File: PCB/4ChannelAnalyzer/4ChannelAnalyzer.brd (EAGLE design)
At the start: 91.5 x 91.4 mm, 19 parts, among them U1 ADS1015IDGST, U2 ADS1015IDGST, U3 LM1117MP-3.3, X3 MINI-USB-32005-301

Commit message: adc's ready signal pins / USB connector
connected adc's ready signal pins to uC and wired USB connector
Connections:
- removed net VDD: U1.8, U2.8
- new net EXT_INT_0: LPC1.42, U1.2
- new net EXT_INT_1: LPC1.43, U2.2
- new net N$15: U1.10
- new net N$16: U1.9
- new net N$17: U2.10
- new net N$18: U2.9
- new net N$19: LPC1.36, X3.2
- new net N$20: LPC1.37, X3.3
- new net USB-5V: X3.1
- new net VCC: U1.1, U1.8, U2.8
- net GND: now also U2.1, X3.5
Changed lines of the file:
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@@
 </elements>
 <signals>
-<signal name="VDD">
-<contactref element="U2" pad="8"/>
-<contactref element="U1" pad="8"/>
-<wire x1="67.31" y1="79.0194" x2="67.31" y2="21.2344" width="0" layer="19" extent="1-1"/>
-</signal>
 <signal name="GND">
 <contactref element="LED4" pad="C"/>
@@
 <contactref element="X1" pad="A4"/>
 <contactref element="X1" pad="A2"/>
-<wire x1="80.05" y1="13.435" x2="67.31" y2="16.8656" width="0" layer="19" extent="1-1"/>
-<wire x1="80.05" y1="18.435" x2="80.05" y2="13.435" width="0" layer="19" extent="1-1"/>
-<wire x1="80.05" y1="23.435" x2="80.05" y2="18.435" width="0" layer="19" extent="1-1"/>
-<wire x1="80.05" y1="28.435" x2="80.05" y2="23.435" width="0" layer="19" extent="1-1"/>
-<wire x1="148.59" y1="20.525" x2="80.05" y2="13.435" width="0" layer="19" extent="1-1"/>
-<wire x1="148.59" y1="28.78" x2="148.59" y2="20.525" width="0" layer="19" extent="1-1"/>
-<wire x1="145.415" y1="39.575" x2="148.59" y2="28.78" width="0" layer="19" extent="1-1"/>
-<wire x1="139.065" y1="49.1" x2="145.415" y2="39.575" width="0" layer="19" extent="1-1"/>
+<contactref element="U2" pad="1"/>
+<contactref element="X3" pad="5"/>
 <wire x1="127.635" y1="49.1" x2="139.065" y2="49.1" width="0" layer="19" extent="1-1"/>
+<wire x1="145.415" y1="39.575" x2="139.065" y2="49.1" width="0" layer="19" extent="1-1"/>
+<wire x1="148.59" y1="28.78" x2="145.415" y2="39.575" width="0" layer="19" extent="1-1"/>
+<wire x1="148.59" y1="20.525" x2="148.59" y2="28.78" width="0" layer="19" extent="1-1"/>
 <wire x1="111.76" y1="54.18" x2="127.635" y2="49.1" width="0" layer="19" extent="1-1"/>
 <wire x1="80.05" y1="70.585" x2="111.76" y2="54.18" width="0" layer="19" extent="1-1"/>
@@
 <wire x1="80.05" y1="80.585" x2="80.05" y2="75.585" width="0" layer="19" extent="1-1"/>
 <wire x1="80.05" y1="85.585" x2="80.05" y2="80.585" width="0" layer="19" extent="1-1"/>
-<wire x1="67.31" y1="74.6506" x2="80.05" y2="70.585" width="0" layer="19" extent="1-1"/>
+<wire x1="67.31" y1="74.6506" x2="80.05" y2="75.585" width="0" layer="19" extent="1-1"/>
+<wire x1="66.3194" y1="74.6506" x2="67.31" y2="74.6506" width="0" layer="19" extent="1-1"/>
+<wire x1="80.05" y1="28.435" x2="111.76" y2="54.18" width="0" layer="19" extent="1-1"/>
+<wire x1="80.05" y1="23.435" x2="80.05" y2="28.435" width="0" layer="19" extent="1-1"/>
+<wire x1="80.05" y1="18.435" x2="80.05" y2="23.435" width="0" layer="19" extent="1-1"/>
+<wire x1="80.05" y1="13.435" x2="80.05" y2="18.435" width="0" layer="19" extent="1-1"/>
+<wire x1="67.31" y1="16.8656" x2="80.05" y2="18.435" width="0" layer="19" extent="1-1"/>
+<wire x1="21.92" y1="7.445" x2="67.31" y2="16.8656" width="0" layer="19" extent="1-1"/>
 </signal>
 <signal name="N$2">
@@
 <wire x1="80.05" y1="25.935" x2="67.818" y2="21.2344" width="0" layer="19" extent="1-1"/>
 </signal>
+<signal name="VCC">
+<contactref element="U1" pad="1"/>
+<contactref element="U1" pad="8"/>
+<contactref element="U2" pad="8"/>
+<wire x1="67.31" y1="21.2344" x2="67.31" y2="79.0194" width="0" layer="19" extent="1-1"/>
+<wire x1="66.3194" y1="16.8656" x2="67.31" y2="21.2344" width="0" layer="19" extent="1-1"/>
+</signal>
+<signal name="EXT_INT_0">
+<contactref element="U1" pad="2"/>
+<contactref element="LPC1" pad="42"/>
+<wire x1="8.255" y1="42.545" x2="66.802" y2="16.8656" width="0" layer="19" extent="1-1"/>
+</signal>
+<signal name="EXT_INT_1">
+<contactref element="U2" pad="2"/>
+<contactref element="LPC1" pad="43"/>
+<wire x1="8.255" y1="45.085" x2="66.802" y2="74.6506" width="0" layer="19" extent="1-1"/>
+</signal>
+<signal name="N$15">
+<contactref element="U1" pad="10"/>
+</signal>
+<signal name="N$16">
+<contactref element="U1" pad="9"/>
+</signal>
+<signal name="N$17">
+<contactref element="U2" pad="10"/>
+</signal>
+<signal name="N$18">
+<contactref element="U2" pad="9"/>
+</signal>
+<signal name="N$19">
+<contactref element="LPC1" pad="36"/>
+<contactref element="X3" pad="2"/>
+<wire x1="19.52" y1="7.445" x2="8.255" y2="27.305" width="0" layer="19" extent="1-1"/>
+</signal>
+<signal name="N$20">
+<contactref element="LPC1" pad="37"/>
+<contactref element="X3" pad="3"/>
+<wire x1="20.32" y1="7.445" x2="8.255" y2="29.845" width="0" layer="19" extent="1-1"/>
+</signal>
+<signal name="USB-5V">
+<contactref element="X3" pad="1"/>
+</signal>
 </signals>

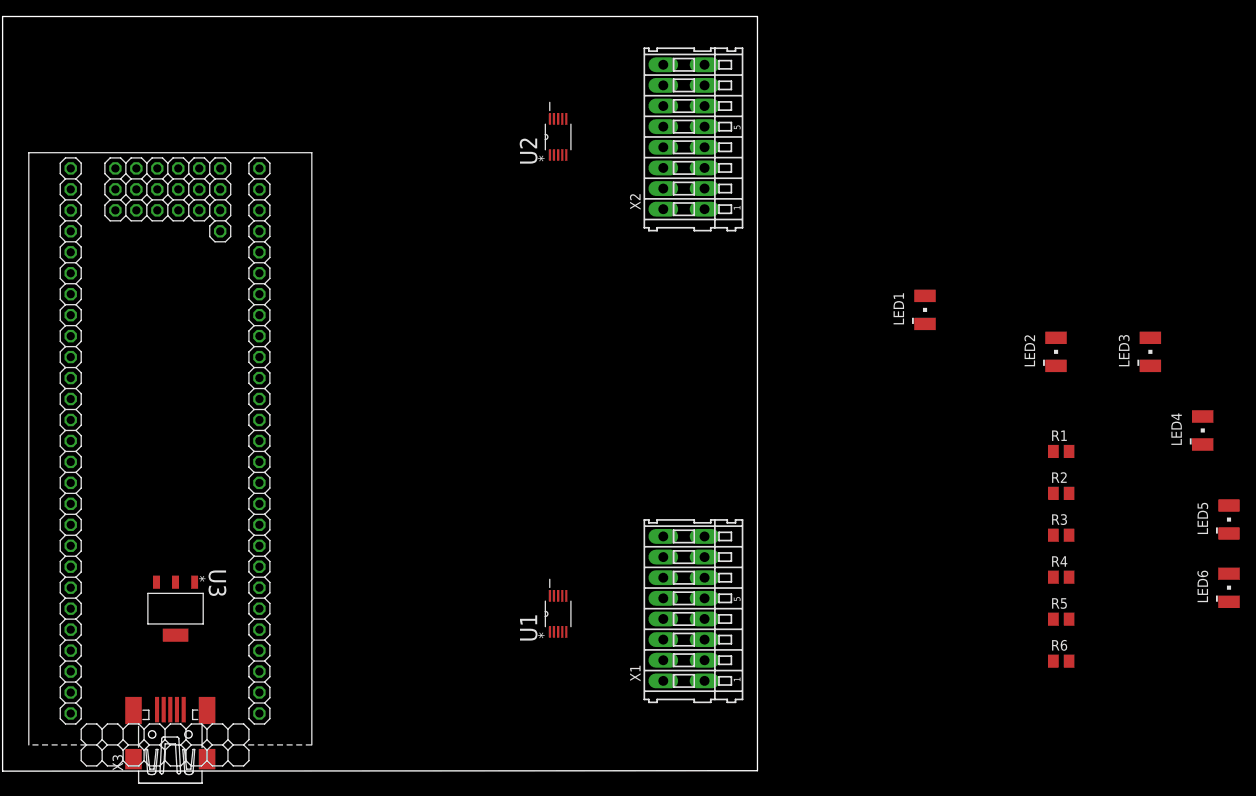
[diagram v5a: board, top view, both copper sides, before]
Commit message: Wired LED signals.
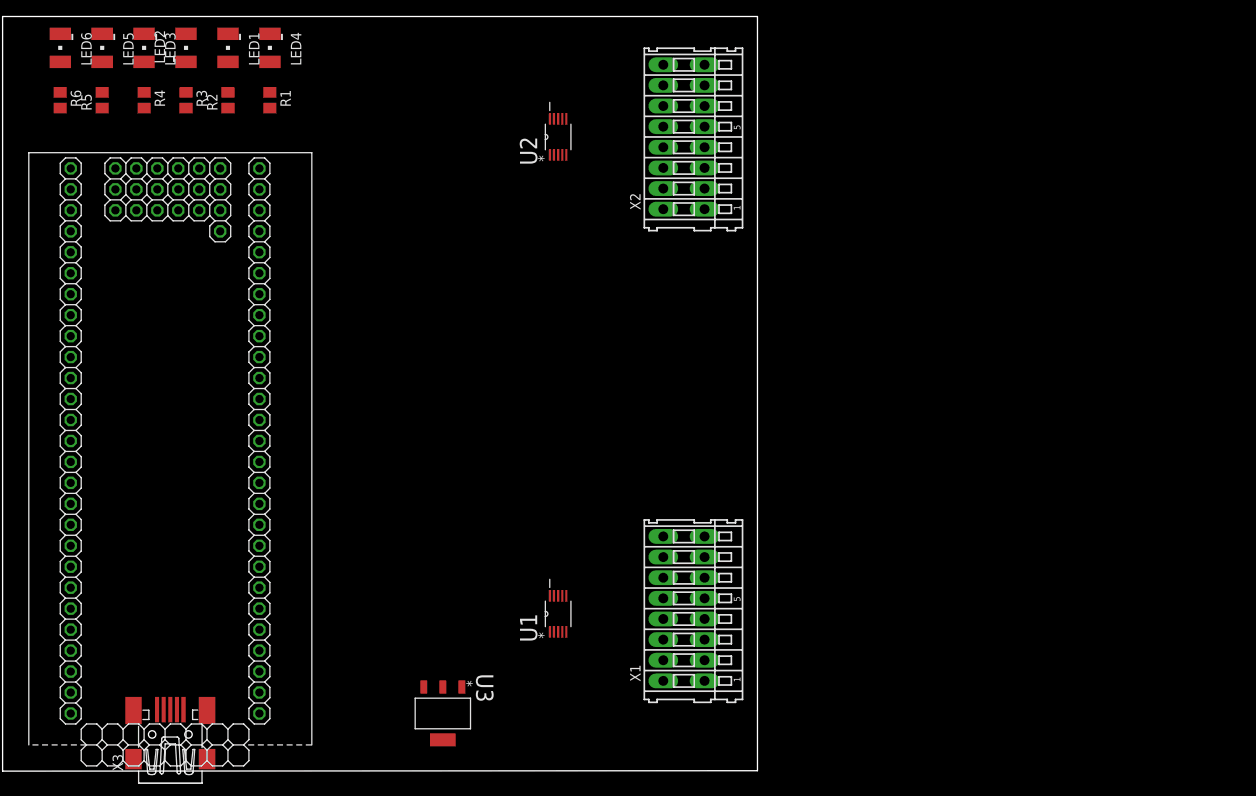
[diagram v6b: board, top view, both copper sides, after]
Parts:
- moved LED6 156.0 mm to (6.99, 87.6), turned to 180 degrees
- moved LED5 148.0 mm to (12.1, 87.6), turned to 180 degrees
- moved R6 139.0 mm to (6.99, 81.3), turned to 270 degrees
- moved R5 132.1 mm to (12.1, 81.3), turned to 90 degrees
- moved LED3 127.4 mm to (17.1, 87.6), turned to 180 degrees
- moved R4 125.3 mm to (17.1, 81.3), turned to 270 degrees
- moved LED4 122.2 mm to (32.4, 87.6), turned to 180 degrees
- moved R3 118.4 mm to (22.2, 81.3), turned to 270 degrees
- moved LED2 111.7 mm to (22.2, 87.6)
- moved R2 111.6 mm to (27.3, 81.3), turned to 90 degrees
- moved R1 104.9 mm to (32.4, 81.3), turned to 270 degrees
- moved LED1 90.2 mm to (27.3, 87.6), turned to 180 degrees
- moved U3 34.8 mm to (53.3, 6.99)
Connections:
- new net N$21: LPC1.58, R1.2
- new net N$22: LPC1.61, R2.2
- new net N$23: LPC1.64, R3.2
- new net N$24: LPC1.67, R4.2
- new net N$25: LPC1.70, R5.2
- new net N$26: LPC1.73, R6.2

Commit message: Conected ADC to uC, wired ADC to connector (in PCB)
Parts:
- removed U1, U2: ADS1015IDGST, ADS1015:SOP50P490X110-10N
- added C1, C2: 10uF, rcl:C0805
- added U1-ADD-49, U2-ADD-48: ADS1015IDGST, ADS1015:SOP50P490X110-10N
- moved U3 25.9 mm to (58.4, 32.4)
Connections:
- removed net N$15: U1.10
- removed net N$16: U1.9
- removed net N$17: U2.10
- removed net N$18: U2.9
- removed net VCC: U1.1, U1.8, U2.8
- new net SCL48: U2-ADD-48.10
- new net SCL49: LPC1.10, U1-ADD-49.10
- new net SDA48: U2-ADD-48.9
- new net SDA49: LPC1.9, U1-ADD-49.9
- new net VCC3.3V: C2.1, LPC1.28, U1-ADD-49.1, U1-ADD-49.8, U2-ADD-48.8, U3.2, U3.4
- net EXT_INT_0: now also U1-ADD-49.2; no longer U1.2
- net EXT_INT_1: now also U2-ADD-48.2; no longer U2.2
- net GND: now also C1.2, C2.2, U1-ADD-49.3, U2-ADD-48.1, U2-ADD-48.3, U3.1; no longer U1.3, U2.1, U2.3
- net N$1: now also U1-ADD-49.4; no longer U1.4
- net N$10: now also U2-ADD-48.5; no longer U2.5
- net N$11: now also U2-ADD-48.6; no longer U2.6
- net N$12: now also U2-ADD-48.7; no longer U2.7
- net N$13: now also U1-ADD-49.6; no longer U1.6
- net N$14: now also U1-ADD-49.7; no longer U1.7
- net N$8: now also U1-ADD-49.5; no longer U1.5
- net N$9: now also U2-ADD-48.4; no longer U2.4
- net USB-5V: now also C1.1, U3.3
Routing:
- net GND: track 0.00 -> 14.8 mm
- net N$9: track 0.00 -> 9.92 mm
- net N$1: track 0.00 -> 9.92 mm
- net N$12: track 0.00 -> 9.53 mm
- net VCC3.3V: track 0.00 -> 9.10 mm
- net N$14: track 0.00 -> 8.79 mm
- net N$13: track 0.00 -> 4.90 mm
- net N$11: track 0.00 -> 4.90 mm
- net N$10: track 0.00 -> 4.89 mm
- net N$8: track 0.00 -> 4.89 mm

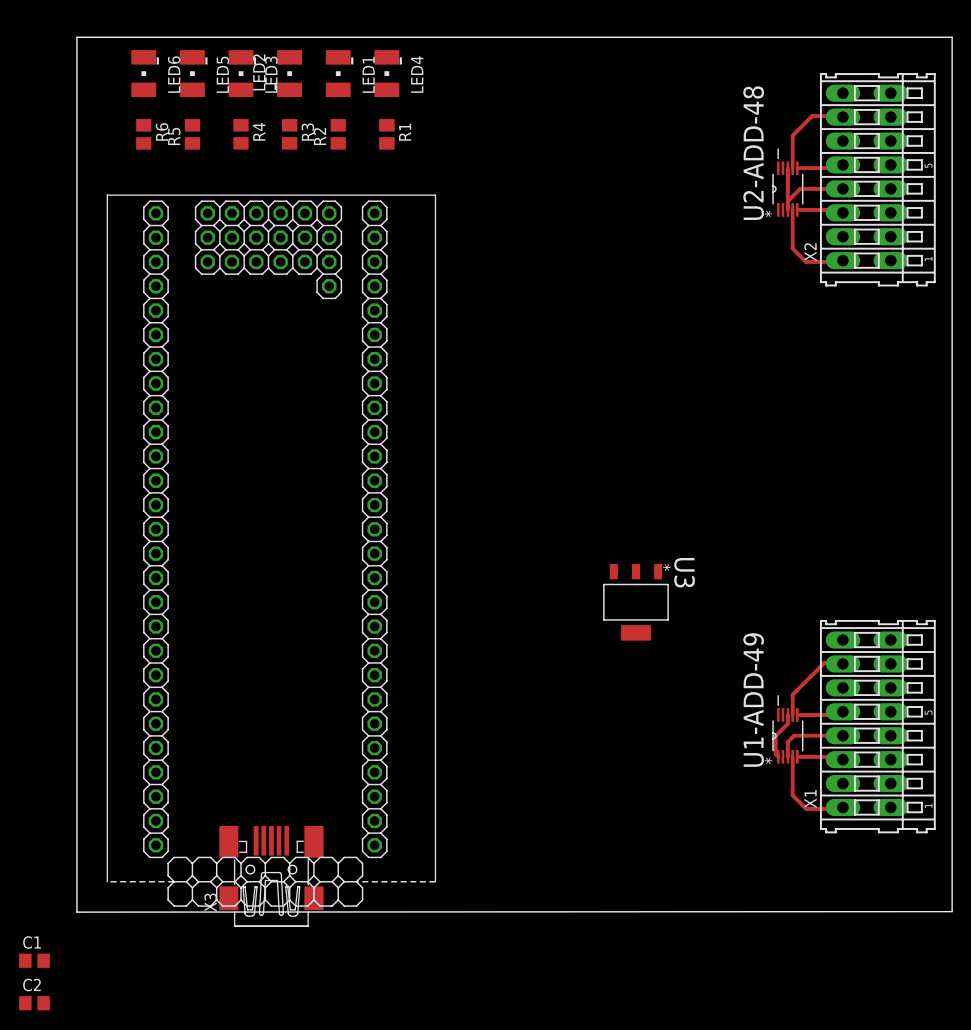
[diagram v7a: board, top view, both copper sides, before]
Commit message: Wiring all components (without power supply)
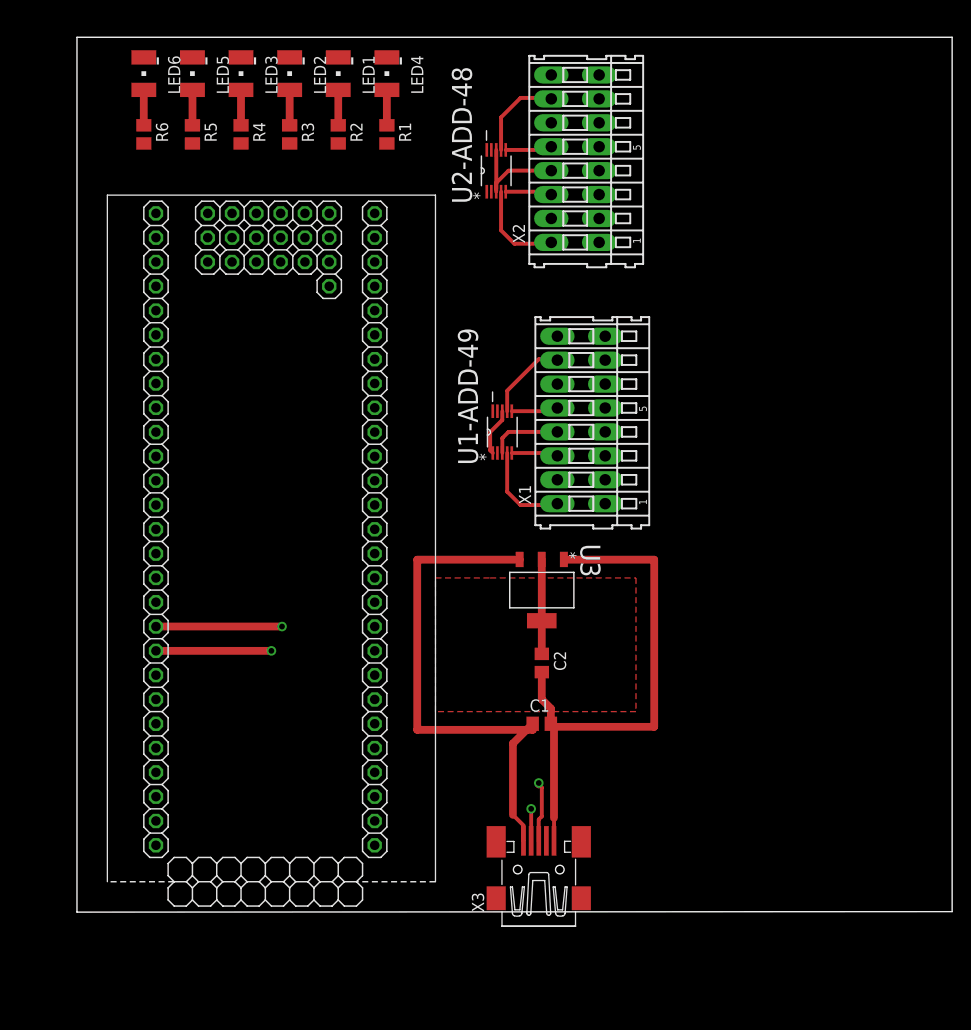
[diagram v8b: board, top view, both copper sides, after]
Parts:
- moved C2 63.8 mm to (48.6, 26.0), turned to 270 degrees
- moved C1 58.5 mm to (48.6, 19.7)
- moved U1-ADD-49 43.6 mm to (44.5, 50.2)
- moved X1 43.6 mm to (52.7, 51.4)
- moved U2-ADD-48 30.5 mm to (43.8, 77.5)
- moved X2 30.5 mm to (52.1, 78.7)
- moved X3 27.9 mm to (48.3, 4.45)
- moved U3 9.92 mm to (48.6, 33.7)
- turned LED2 to 180 degrees
- turned R2 to 270 degrees
- turned R5 to 270 degrees
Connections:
- net SCL48: now also LPC1.56
- net SDA48: now also LPC1.57
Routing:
- net GND: track 14.8 -> 70.4 mm
- net USB-5V: track 0.00 -> 54.8 mm
- net N$20: track 0.00 -> 19.5 mm, vias 0 -> 2
- net N$19: track 0.00 -> 15.4 mm, vias 0 -> 2
- net VCC3.3V: track 9.10 -> 19.0 mm
- net N$7: track 0.00 -> 3.70 mm
- net N$6: track 0.00 -> 3.70 mm
- net N$5: track 0.00 -> 3.70 mm
- net N$4: track 0.00 -> 3.70 mm
- net N$3: track 0.00 -> 3.70 mm
- net N$2: track 0.00 -> 3.70 mm
- added copper zone on layer 1, net VCC3.3V
